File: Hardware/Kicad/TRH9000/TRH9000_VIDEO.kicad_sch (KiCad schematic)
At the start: 32 parts, among them J1 RGB, J2 Console5_SCART, Q1 BC817, U6 LMH1980

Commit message: Routing, readme, etc
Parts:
- J2, R27, R28, R29: now left out of the parts list
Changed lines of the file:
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@@
   )
   (symbol (lib_id "LRJ-parts:Console5_SCART") (at 265.43 81.28 0) (unit 1)
-    (in_bom yes) (on_board yes)
+    (in_bom no) (on_board no)
     (property "Reference" "J2" (id 0) (at 256.54 46.99 0))
     (property "Value" "Console5_SCART" (id 1) (at 246.38 111.76 0))
@@
   )
   (symbol (lib_id "Device:R") (at 240.03 81.28 270) (unit 1)
-    (in_bom yes) (on_board yes)
+    (in_bom no) (on_board no)
     (property "Reference" "R29" (id 0) (at 234.95 80.01 90))
     (property "Value" "1k" (id 1) (at 240.03 81.28 90))
@@
   )
   (symbol (lib_id "Device:R") (at 234.95 40.64 0) (mirror y) (unit 1)
-    (in_bom yes) (on_board yes)
+    (in_bom no) (on_board no)
     (property "Reference" "R27" (id 0) (at 232.918 40.64 90))
     (property "Value" "100" (id 1) (at 234.95 40.64 90))
@@
   )
   (symbol (lib_id "Device:R") (at 234.95 50.8 0) (mirror y) (unit 1)
-    (in_bom yes) (on_board yes)
+    (in_bom no) (on_board no)
     (property "Reference" "R28" (id 0) (at 232.918 50.8 90))
     (property "Value" "100" (id 1) (at 234.95 50.8 90))

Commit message: Multiple changes. Check the dev log.
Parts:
- removed J2: Console5_SCART, LRJ:SCART-21_Female_Horizontal_P1.905x2.54mm_EdgePinOffset10.7mm, symbol LRJ-parts:Console5_SCART
- removed R27, R28: 100, Resistor_SMD:R_0603_1608Metric, symbol Device:R
- removed R29: 1k, Resistor_SMD:R_0603_1608Metric, symbol Device:R
- added J2: RGB, Connector_Dsub:DSUB-15-HD_Female_Horizontal_P2.29x1.98mm_EdgePinOffset3.03mm_Housed_MountingHolesOffset4.94mm, symbol Connector:DB15_Female
- added SW1: SW_DP3T, Switches:SWITCH_SP3T_SMD, symbol Switch:SW_DP3T
- added U7: ICL7660, Package_SO:SOP-8_3.9x4.9mm_P1.27mm, symbol Regulator_SwitchedCapacitor:ICL7660
- added U8: LT1675, Package_SO:SSOP-16_3.9x4.9mm_P0.635mm, symbol TRH9000:LT1675
- renumbered C33 to C10, C34 to C11, C19 to C12, C20 to C13, C21 to C14, C13 to C15, C17 to C5, C14 to C6, C15 to C7, C16 to C8, C32 to C9, R9 to R10, R10 to R11, R24 to R12, R25 to R13, R26 to R14, R17 to R15, R18 to R16, R19 to R17, R12 to R7, R13 to R8, R15 to R9
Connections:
- no-connect marks 16 -> 9
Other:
- note added: "Superimposer"
- note added: "Video Connectors"
- note removed: "Loading Blank with 2.5V signals to the Monitor that the Scart is in RGB-mode."
- note removed: "Video Output Connectors"

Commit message: Multiple changes.
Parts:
- removed J2: RGB, Connector_Dsub:DSUB-15-HD_Female_Horizontal_P2.29x1.98mm_EdgePinOffset3.03mm_Housed_MountingHolesOffset4.94mm, symbol Connector:DB15_Female
- removed SW1: SW_DP3T, Switches:SWITCH_SP3T_SMD, symbol Switch:SW_DP3T
- removed U7: ICL7660, Package_SO:SOP-8_3.9x4.9mm_P1.27mm, symbol Regulator_SwitchedCapacitor:ICL7660
- removed U8: LT1675, Package_SO:SSOP-16_3.9x4.9mm_P0.635mm, symbol TRH9000:LT1675
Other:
- note removed: "Implementing Superimpose: ----------------------- 1. Feed external HSYNC / VSYNC into V9990 HRESET / VRESET pins for synchronisation 2. Combine external and internal R, G, B with an analog multiplexer, controlled by /Ys signal The principle is that the original external signal is passed through while /Ys is not superimposing."
- note removed: "Superimposer"
- moved on the sheet: C10, C11, C12, C13, C14, C15, C5, C6, C7, C8, C9, J1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

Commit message: Multiple changes.
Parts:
- removed C11: 0.1µF, Capacitor_SMD:C_0805_2012Metric, symbol LRJ-parts:C_CL10B104KB8NNNL
- removed C15: 10µF, Capacitor_SMD:C_0805_2012Metric, symbol LRJ-parts:C_GRM188D71A106KA73D
- removed R12: 10k, Capacitor_SMD:C_0805_2012Metric, symbol LRJ-parts:R_RC0603FR-0710KL
- added C11: 0.1uF, Capacitor_SMD:C_0805_2012Metric, symbol Device:C
- added C15: 10uF, Capacitor_SMD:C_0805_2012Metric, symbol Device:C
- added R12: 10K, Resistor_SMD:R_0805_2012Metric, symbol Device:R
- C12, C13, C14: footprint Capacitor_THT:CP_Radial_D5.0mm_P2.50mm -> Capacitor_Tantalum_SMD:CP_EIA-3528-15_AVX-H
- C5: value 220uF -> 220uF 6.3V; footprint Capacitor_THT:CP_Radial_D5.0mm_P2.50mm -> Capacitor_Tantalum_SMD:CP_EIA-3528-15_AVX-H; Case (none) -> B
- U6: symbol LRJ-parts:LMH1980 -> TRH9000:LMH1980
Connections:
- net GND: now also C15.2, R12.2
- net GND1: now also C15.1
- net SYNCIN: now also C11.2
- net at C10.1, C9.1, R11.1: now also C11.1
- net at U6.1 (REXT): now also R12.1
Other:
- moved on the sheet: C5, Q1, R7, R8

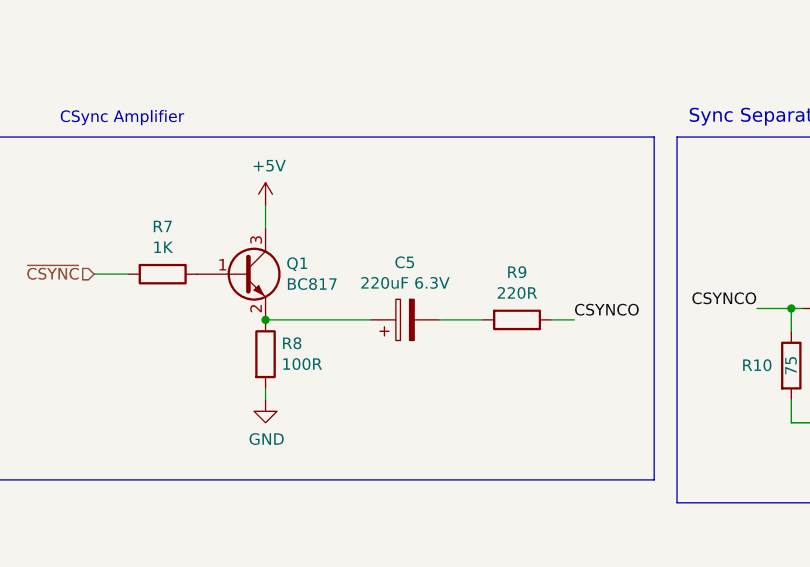
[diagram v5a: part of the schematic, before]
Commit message: Moving caps to avoid conflict with sockets, uploading image with issue when superimposing
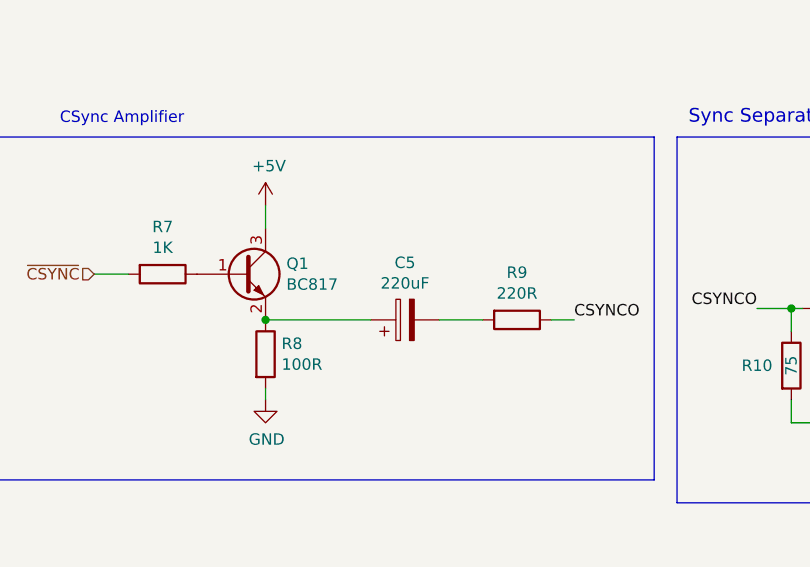
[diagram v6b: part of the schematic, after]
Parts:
- C5: value 220uF 6.3V -> 220uF
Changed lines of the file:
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@@
     (in_bom yes) (on_board yes)
     (property "Reference" "C5" (id 0) (at 118.364 179.07 90))
-    (property "Value" "220uF 6.3V" (id 1) (at 118.364 181.356 90))
+    (property "Value" "220uF" (id 1) (at 118.364 181.356 90))
     (property "Footprint" "Capacitor_Tantalum_SMD:CP_EIA-3528-15_AVX-H" (id 2) (at 122.174 184.4548 0)
       (effects (font (size 1.27 1.27)) hide)
